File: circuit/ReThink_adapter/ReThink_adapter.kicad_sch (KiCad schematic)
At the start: 69 parts, among them J1 FH34SRJ-34S-0.5SH(50), J2 FH34SRJ-6S-0.5SH(50), J3 Mezzanine, J4 XF3M(1)-3015-1B, J5 XF3M(1)-0815-1B, J6 FH34SRJ-40S-0.5SH(50), J7 FH52-40S-0.5SH, J8 XF3M(1)-1415-1B, U1 PCAL6416AHF, U2 LM2775DSG, U3 PCA9306, U4 TPS610333DRLR

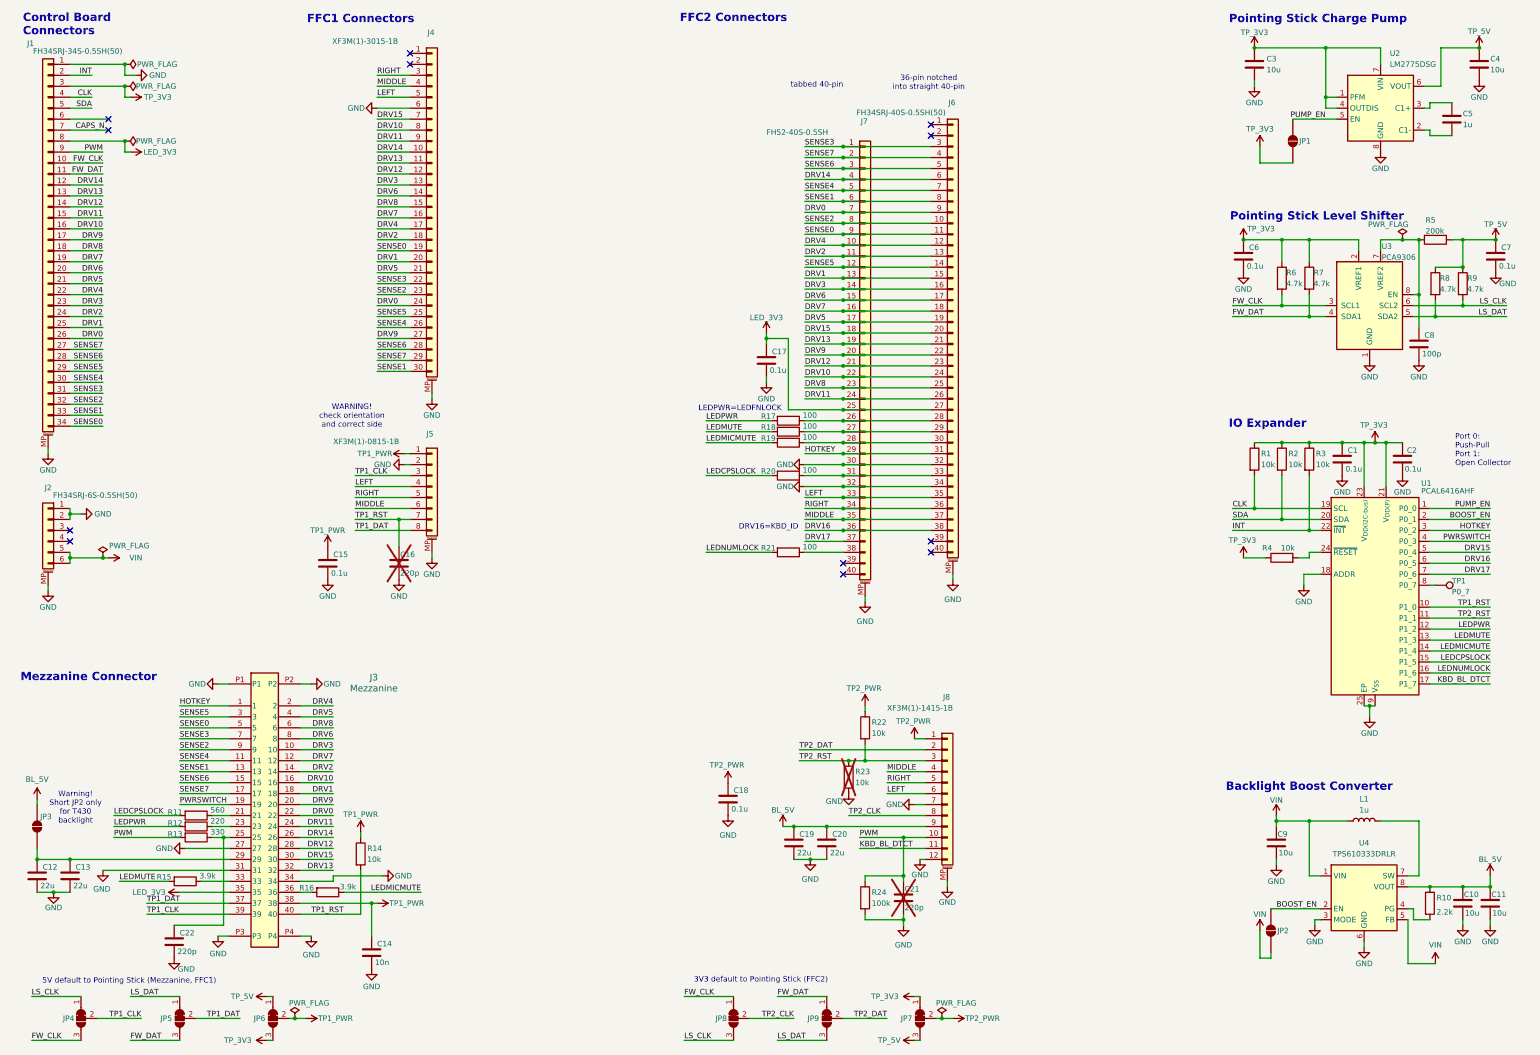
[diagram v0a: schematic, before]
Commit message: group connectors on PCB
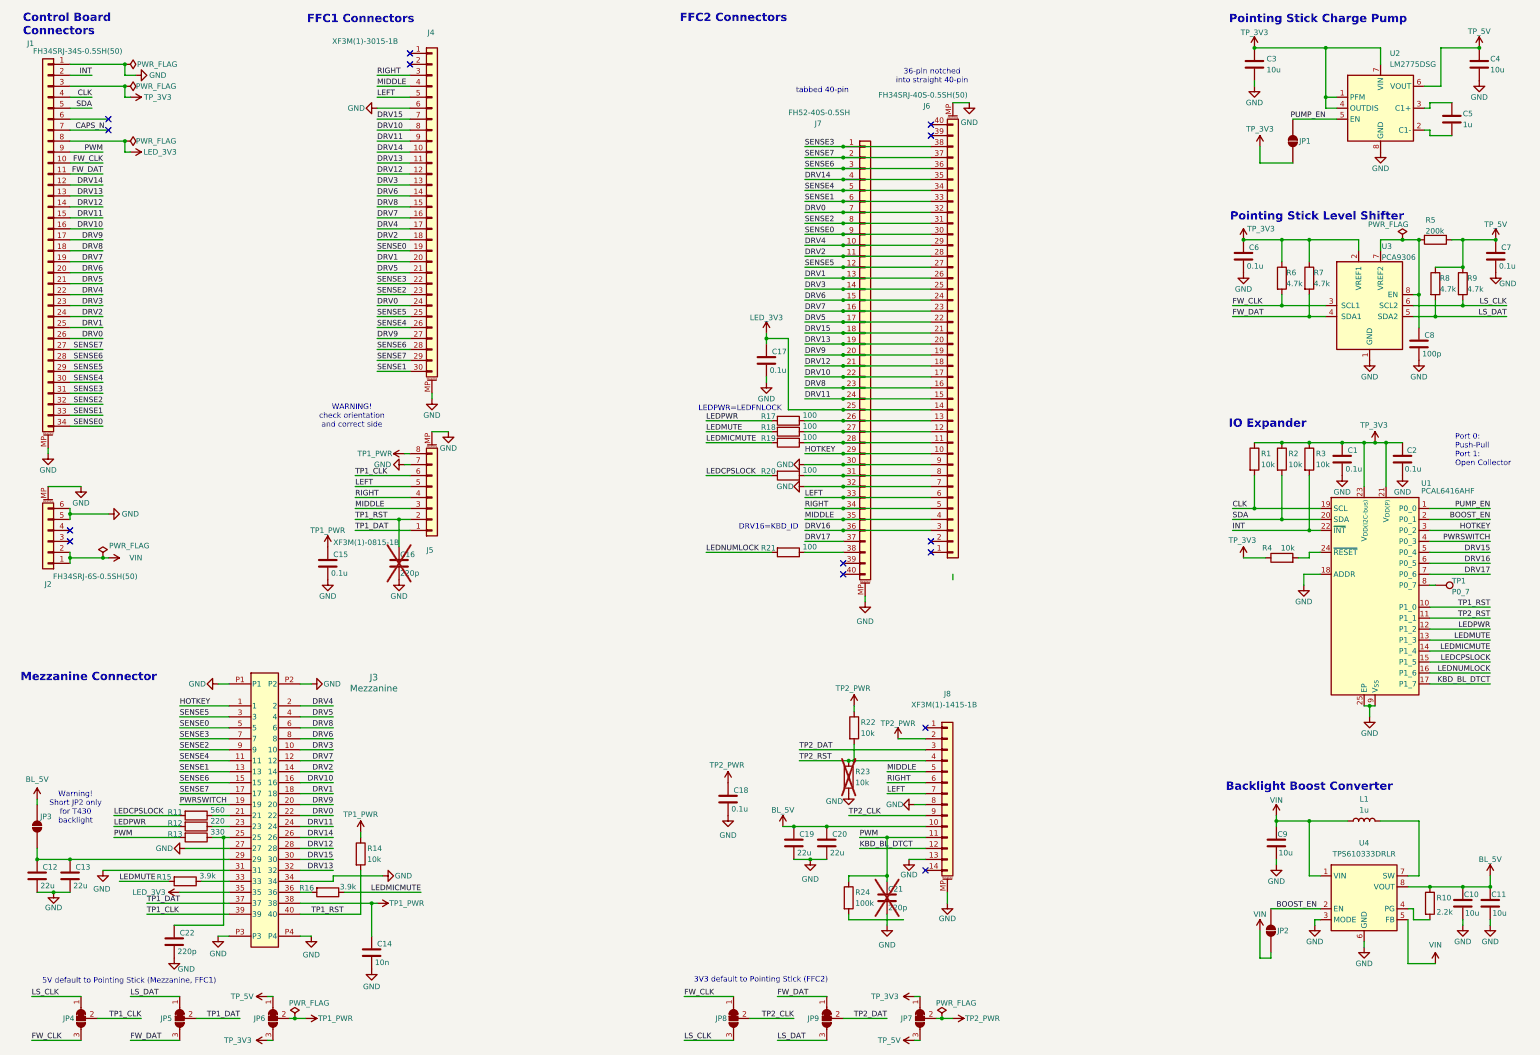
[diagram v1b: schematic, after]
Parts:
- J8: symbol Connector_Generic_MountingPin:Conn_01x12_MountingPin -> Connector_Generic_MountingPin:Conn_01x14_MountingPin
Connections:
- net BL_5V: now also J8.10 (Pin_10); no longer J8.9 (Pin_9)
- net DRV0: now also J6.32 (Pin_32); no longer J6.9 (Pin_9)
- net DRV1: now also J6.26 (Pin_26); no longer J6.15 (Pin_15)
- net DRV10: now also J6.17 (Pin_17); no longer J6.24 (Pin_24)
- net DRV11: now also J6.15 (Pin_15); no longer J6.26 (Pin_26)
- net DRV12: now also J6.18 (Pin_18); no longer J6.23 (Pin_23)
- net DRV13: now also J6.20 (Pin_20); no longer J6.21 (Pin_21)
- net DRV14: now also J6.35 (Pin_35); no longer J6.6 (Pin_6)
- net DRV15: now also J6.21 (Pin_21); no longer J6.20 (Pin_20)
- net DRV16: now also J6.3 (Pin_3); no longer J6.38 (Pin_38)
- net DRV2: now also J6.28 (Pin_28); no longer J6.13 (Pin_13)
- net DRV3: now also J6.25 (Pin_25); no longer J6.16 (Pin_16)
- net DRV4: now also J6.29 (Pin_29); no longer J6.12 (Pin_12)
- net DRV5: now also J6.22 (Pin_22); no longer J6.19 (Pin_19)
- net DRV6: now also J6.24 (Pin_24); no longer J6.17 (Pin_17)
- net DRV7: now also J6.23 (Pin_23); no longer J6.18 (Pin_18)
- net DRV8: now also J6.16 (Pin_16); no longer J6.25 (Pin_25)
- net DRV9: now also J6.19 (Pin_19); no longer J6.22 (Pin_22)
- net GND: now also J2.5 (Pin_5), J2.6 (Pin_6), J5.7 (Pin_7), J6.7 (Pin_7), J6.9 (Pin_9), J8.13 (Pin_13), J8.8 (Pin_8); no longer J2.1 (Pin_1), J2.2 (Pin_2), J5.2 (Pin_2), J6.32 (Pin_32), J6.34 (Pin_34), J8.12 (Pin_12), J8.7 (Pin_7), R24.2
- net HOTKEY: now also J6.10 (Pin_10); no longer J6.31 (Pin_31)
- net KBD_BL_DTCT: now also J8.12 (Pin_12); no longer J8.11 (Pin_11)
- net LED_3V3: now also J6.14 (Pin_14); no longer J6.27 (Pin_27)
- net LEFT: now also J5.5 (Pin_5), J6.6 (Pin_6), J8.7 (Pin_7); no longer J5.4 (Pin_4), J6.35 (Pin_35), J8.6 (Pin_6)
- net MIDDLE: now also J5.3 (Pin_3), J6.4 (Pin_4), J8.5 (Pin_5); no longer J5.6 (Pin_6), J6.37 (Pin_37), J8.4 (Pin_4)
- net PWM: now also J8.11 (Pin_11); no longer J8.10 (Pin_10)
- net RIGHT: now also J5.4 (Pin_4), J6.5 (Pin_5), J8.6 (Pin_6); no longer J5.5 (Pin_5), J6.36 (Pin_36), J8.5 (Pin_5)
- net SENSE0: now also J6.30 (Pin_30); no longer J6.11 (Pin_11)
- net SENSE1: now also J6.33 (Pin_33); no longer J6.8 (Pin_8)
- net SENSE2: now also J6.31 (Pin_31); no longer J6.10 (Pin_10)
- net SENSE3: now also J6.38 (Pin_38); no longer J6.3 (Pin_3)
- net SENSE4: now also J6.34 (Pin_34); no longer J6.7 (Pin_7)
- net SENSE5: now also J6.27 (Pin_27); no longer J6.14 (Pin_14)
- net SENSE6: now also J6.36 (Pin_36); no longer J6.5 (Pin_5)
- net SENSE7: now also J6.37 (Pin_37); no longer J6.4 (Pin_4)
- net TP1_CLK: now also J5.6 (Pin_6); no longer J5.3 (Pin_3)
- net TP1_DAT: now also J5.1 (Pin_1); no longer J5.8 (Pin_8)
- net TP1_PWR: now also J5.8 (Pin_8); no longer J5.1 (Pin_1)
- net TP1_RST: now also J5.2 (Pin_2); no longer J5.7 (Pin_7)
- net TP2_CLK: now also J8.9 (Pin_9); no longer J8.8 (Pin_8)
- net TP2_DAT: now also J8.3 (Pin_3); no longer J8.2 (Pin_2)
- net TP2_PWR: now also J8.2 (Pin_2); no longer J8.1 (Pin_1)
- net TP2_RST: now also J8.4 (Pin_4); no longer J8.3 (Pin_3)
- net VIN: now also J2.1 (Pin_1), J2.2 (Pin_2); no longer J2.5 (Pin_5), J2.6 (Pin_6)
- net at J7.27 (Pin_27), R18.1: now also J6.12 (Pin_12); no longer J6.29 (Pin_29)
- net at J7.26 (Pin_26), R17.1: now also J6.13 (Pin_13); no longer J6.28 (Pin_28)
- net at J7.28 (Pin_28), R19.1: now also J6.11 (Pin_11); no longer J6.30 (Pin_30)
- net at J7.31 (Pin_31), R20.1: now also J6.8 (Pin_8); no longer J6.33 (Pin_33)
- no-connect marks 12 -> 14
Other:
- moved on the sheet: C21, J2, J5, J6, R22, R24

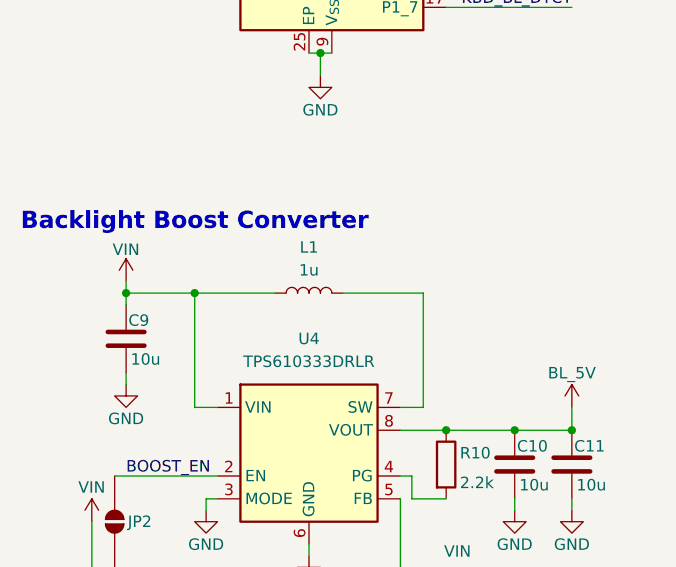
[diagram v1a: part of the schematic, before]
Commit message: added JLCPCB rules
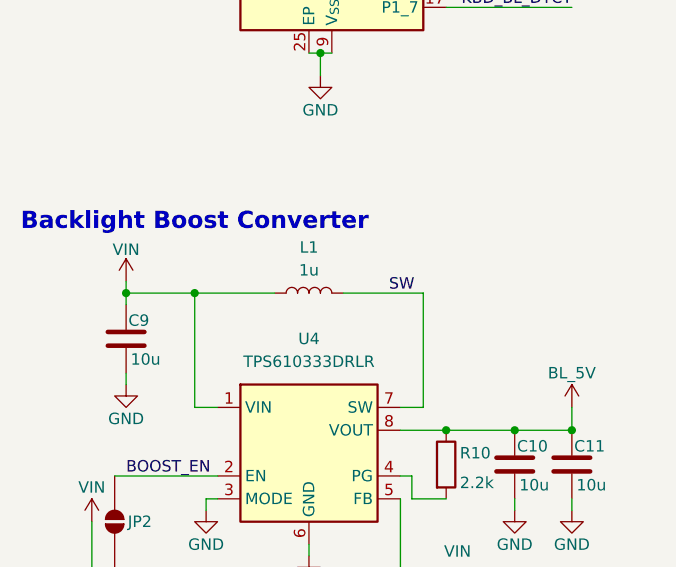
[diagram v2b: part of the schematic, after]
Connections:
- net SW: now reaches L1.2, U4.7 (SW)
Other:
- company: (none) -> Ziemniaczenka
- title: (none) -> ReThink Adapter
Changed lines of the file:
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@@
 	(generator_version "10.0")
 	(paper "A3")
+	(title_block
+		(title "ReThink Adapter")
+		(date "2026-09-30")
+		(rev "V0.1")
+		(company "Ziemniaczenka")
+		(comment 1 "To view a copy of this license, visit https://creativecommons.org/licenses/by-sa/4.0/")
+		(comment 2 "ReThink keyboard by Ziemniaczenka is licensed under CC BY-SA 4.0.")
+	)
 	(text "IO Expander"
 		(exclude_from_sim no)
@@
 		(effects
 			(font
+				(size 1.27 1.27)
+			)
+			(justify left bottom)
+		)
+	)
+	(label "SW"
+		(at 345.44 213.36 0)
+		(effects
+			(font

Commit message: lock connector placement on adapter PCB
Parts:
- U2: footprint Package_SON:Texas_DSG0008A_WSON-8-1EP_2x2mm_P0.5mm_EP0.9x1.6mm_ThermalVias -> Package_SON:Texas_DSG0008A_WSON-8-1EP_2x2mm_P0.5mm_EP0.9x1.6mm
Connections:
- net GND: now also R24.2
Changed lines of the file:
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@@
 	)
 	(junction
+		(at 226.06 236.22)
+		(diameter 0)
+		(color 0 0 0 0)
+	)
+	(junction
 		(at 363.22 34.29)
 		(diameter 0)
@@
 	(wire
 		(pts
-			(xy 226.06 234.95) (xy 226.06 237.49)
+			(xy 226.06 234.95) (xy 226.06 236.22)
 		)
 		(stroke
@@
 	(wire
 		(pts
-			(xy 217.17 236.22) (xy 229.87 236.22)
+			(xy 217.17 236.22) (xy 226.06 236.22)
 		)
 		(stroke
@@
 	(wire
 		(pts
+			(xy 226.06 236.22) (xy 226.06 237.49)
+		)
+		(stroke
+			(width 0)
+			(type default)
+		)
+	)
+	(wire
+		(pts
 			(xy 207.01 90.17) (xy 215.9 90.17)
 		)
@@
 			)
 		)
-		(property "Footprint" "Package_SON:Texas_DSG0008A_WSON-8-1EP_2x2mm_P0.5mm_EP0.9x1.6mm_ThermalVias"
+		(property "Footprint" "Package_SON:Texas_DSG0008A_WSON-8-1EP_2x2mm_P0.5mm_EP0.9x1.6mm"
 			(at 340.36 48.26 0)
 			(hide yes)

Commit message: start routing
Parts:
- added C23: 0.1u, Capacitor_SMD:C_0402_1005Metric, symbol Device:C
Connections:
- net GND: now also C23.2
- net LED_3V3: now also C23.1
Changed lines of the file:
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@@
 	)
 	(junction
+		(at 191.77 101.6)
+		(diameter 0)
+		(color 0 0 0 0)
+	)
+	(junction
 		(at 349.25 78.74)
 		(diameter 0)
@@
 	(wire
 		(pts
+			(xy 191.77 101.6) (xy 198.12 101.6)
+		)
+		(stroke
+			(width 0)
+			(type default)
+		)
+	)
+	(wire
+		(pts
 			(xy 49.53 38.1) (xy 49.53 40.64)
 		)
@@
 	(wire
 		(pts
+			(xy 191.77 102.87) (xy 191.77 101.6)
+		)
+		(stroke
+			(width 0)
+			(type default)
+		)
+	)
+	(wire
+		(pts
 			(xy 207.01 92.71) (xy 215.9 92.71)
 		)
@@
 	(wire
 		(pts
-			(xy 198.12 100.33) (xy 198.12 101.6)
+			(xy 191.77 100.33) (xy 191.77 101.6)
 		)
 		(stroke
@@
 	(wire
 		(pts
+			(xy 191.77 111.76) (xy 191.77 110.49)
+		)
+		(stroke
+			(width 0)
+			(type default)
+		)
+	)
+	(wire
+		(pts
 			(xy 27.94 254) (xy 39.37 254)
 		)
@@
 	(symbol
 		(lib_id "power:+3V3")
-		(at 198.12 100.33 0)
+		(at 191.77 100.33 0)
 		(mirror y)
 		(unit 1)
@@
 		(dnp no)
 		(property "Reference" "#PWR055"
-			(at 198.12 104.14 0)
+			(at 191.77 104.14 0)
 			(hide yes)
 			(show_name no)
@@
 		)
 		(property "Value" "LED_3V3"
-			(at 198.12 96.774 0)
+			(at 191.77 96.774 0)
 			(show_name no)
 			(do_not_autoplace no)
@@
 		)
 		(property "Footprint" ""
-			(at 198.12 100.33 0)
+			(at 191.77 100.33 0)
 			(hide yes)
 			(show_name no)
@@
 		)
 		(property "Datasheet" ""
-			(at 198.12 100.33 0)
+			(at 191.77 100.33 0)
 			(hide yes)
 			(show_name no)
@@
 		)
 		(property "Description" "Power symbol creates a global label with name \"+3V3\""
-			(at 198.12 100.33 0)
+			(at 191.77 100.33 0)
 			(hide yes)
 			(show_name no)
@@
 	)
 	(symbol
+		(lib_id "power:GND")
+		(at 191.77 111.76 0)
+		(mirror y)
+		(unit 1)
+		(body_style 1)
+		(exclude_from_sim no)
+		(in_bom yes)
+		(on_board yes)
+		(in_pos_files yes)
+		(dnp no)
+		(property "Reference" "#PWR080"
+			(at 191.77 118.11 0)
+			(hide yes)
+			(show_name no)
+			(do_not_autoplace no)
+			(effects
+				(font
+					(size 1.27 1.27)
+				)
+			)
+		)
+		(property "Value" "GND"
+			(at 191.77 115.57 0)
+			(show_name no)
+			(do_not_autoplace no)
+			(effects
+				(font
+					(size 1.27 1.27)
+				)
+			)
+		)
+		(property "Footprint" ""
+			(at 191.77 111.76 0)
+			(hide yes)
+			(show_name no)
+			(do_not_autoplace no)
+			(effects
+				(font
+					(size 1.27 1.27)
+				)
+			)
+		)
+		(property "Datasheet" ""
+			(at 191.77 111.76 0)
+			(hide yes)
+			(show_name no)
+			(do_not_autoplace no)
+			(effects
+				(font
+					(size 1.27 1.27)
+				)
+			)
+		)
+		(property "Description" "Power symbol creates a global label with name \"GND\" , ground"
+			(at 191.77 111.76 0)
+			(hide yes)
+			(show_name no)
+			(do_not_autoplace no)
+			(effects
+				(font
+					(size 1.27 1.27)
+				)
+			)
+		)
+		(pin "1"
+		)
+		(instances
+			(project "ReThink_adapter"
+				(path "/6cef7f30-4344-4878-be02-7aa54a02ef81"
+					(reference "#PWR080")
+					(unit 1)
+				)
+			)
+		)
+	)
+	(symbol
 		(lib_id "ReThink_symbols:543630489")
 		(at 82.55 210.82 0)
@@
 					(unit 1)
 				)
+			)
+		)
+	)
+	(symbol
+		(lib_id "Device:C")
+		(at 191.77 106.68 0)
+		(unit 1)
+		(body_style 1)
+		(exclude_from_sim no)
+		(in_bom yes)
+		(on_board yes)
+		(in_pos_files yes)
+		(dnp no)
+		(property "Reference" "C23"
+			(at 193.04 104.648 0)
+			(show_name no)
+			(do_not_autoplace no)
+			(effects
+				(font
+					(size 1.27 1.27)
+				)
+				(justify left)
+			)
+		)
+		(property "Value" "0.1u"
+			(at 192.532 108.966 0)
+			(show_name no)
+			(do_not_autoplace no)
+			(effects
+				(font
+					(size 1.27 1.27)
+				)
+				(justify left)
+			)
+		)
+		(property "Footprint" "Capacitor_SMD:C_0402_1005Metric"
+			(at 192.7352 110.49 0)
+			(hide yes)
+			(show_name no)
+			(do_not_autoplace no)
+			(effects
+				(font
+					(size 1.27 1.27)
+				)
+			)
+		)
+		(property "Datasheet" ""
+			(at 191.77 106.68 0)
+			(hide yes)
+			(show_name no)
+			(do_not_autoplace no)
+			(effects
+				(font
+					(size 1.27 1.27)
+				)
+			)
+		)
+		(property "Description" "Unpolarized capacitor"
+			(at 191.77 106.68 0)
+			(hide yes)
+			(show_name no)
+			(do_not_autoplace no)
+			(effects
+				(font
+					(size 1.27 1.27)
+				)
+			)
+		)
+		(property "Dielectric" "X7R"
+			(at 191.77 106.68 0)
+			(hide yes)
+			(show_name no)
+			(do_not_autoplace no)
+			(effects
+				(font
+					(size 1.27 1.27)
+				)
+			)
+		)
+		(property "Voltage" "16"
+			(at 191.77 106.68 0)
+			(hide yes)
+			(show_name no)
+			(do_not_autoplace no)
+			(effects
+				(font
+					(size 1.27 1.27)
+				)
+			)
+		)
+		(property "MPN" ""
+			(at 191.77 106.68 0)
+			(hide yes)
+			(show_name no)
+			(do_not_autoplace no)
+			(effects
+				(font
+					(size 1.27 1.27)
+				)
+			)
+		)
+		(pin "2"
+		)
+		(pin "1"
+		)
+		(instances
+			(project "ReThink_adapter"
+				(path "/6cef7f30-4344-4878-be02-7aa54a02ef81"
+					(reference "C23")
+					(unit 1)
+				)

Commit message: routing mostly done
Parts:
- added H1, H2, H3, H4: M2.5, MountingHole:MountingHole_2.7mm_M2.5_DIN965_Pad, symbol Mechanical:MountingHole_Pad
- added H5, H6: M2, MountingHole:MountingHole_2.2mm_M2_ISO14580, symbol Mechanical:MountingHole
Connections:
- net GND: now also H1.1, H2.1, H3.1, H4.1
- net LEFT renamed TP2_LEFT
- net TP2_LEFT: no longer J4.5 (Pin_5), J5.5 (Pin_5)
- net MIDDLE renamed TP2_MIDDLE
- net TP2_MIDDLE: no longer J4.4 (Pin_4), J5.3 (Pin_3)
- net RIGHT renamed TP2_RIGHT
- net TP2_RIGHT: no longer J4.3 (Pin_3), J5.4 (Pin_4)
- new net TP1_LEFT: J4.5 (Pin_5), J5.5 (Pin_5)
- new net TP1_MIDDLE: J4.4 (Pin_4), J5.3 (Pin_3)
- new net TP1_RIGHT: J4.3 (Pin_3), J5.4 (Pin_4)
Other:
- note added: "Mounting holes"

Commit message: finish routing
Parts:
- removed TP1: P0_7, TestPoint:TestPoint_THTPad_D1.5mm_Drill0.7mm, symbol Connector:TestPoint
- added J10: OUT2, Connector_PinHeader_2.54mm:PinHeader_1x02_P2.54mm_Vertical, symbol Connector_Generic:Conn_01x02
- added J11: OUT3, Connector_PinHeader_2.54mm:PinHeader_1x02_P2.54mm_Vertical, symbol Connector_Generic:Conn_01x02
- added J9: OUT1, Connector_PinHeader_2.54mm:PinHeader_1x02_P2.54mm_Vertical, symbol Connector_Generic:Conn_01x02
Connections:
- net BL_5V: now also J10.1 (Pin_1)
- net GND: now also J10.2 (Pin_2), J11.2 (Pin_2), J9.2 (Pin_2)
- net LED_3V3: now also J11.1 (Pin_1)
- net at U1.8 (P0_7): now also J9.1 (Pin_1)
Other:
- moved on the sheet: C12, C13, C14, C17, C18, C19, C20, C21, C22, C23, H1, H2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
